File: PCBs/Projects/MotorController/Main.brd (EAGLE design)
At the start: 172.7 x 115.2 mm, 112 parts, among them Q1 ZXMP10A17GQ, Q2 BUK9240-100A.118, Q3 BUK9240-100A.118, Q4 MMBT5551LT1G, U1 LT4356-2, U2 DRV8301, U3 ESDA6V1SC6Y, U4 MTI85W100GC, U5 ESDA6V1SC6Y, U7 ESDA6V1SC6Y, U8 TMP101, U9 ACS758LCB

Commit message: Schematic in eagle finished -decided to stick with eagle for the time being since the kicad switchover would take a lot of time -freewheeling diodes switched to vertical packages -footprint for psoc module completed -inductor package fixed -rgb led decided on and part made -changed abc order of connector j3 -part renumbering
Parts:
- removed 10U: 47u, SparkFun-Capacitors:1210
- removed D14: LED-RGB-CC-THRUDIFFUSE, SparkFun-LED:LED-RGB-THRU
- removed H1, H2, H3, H4, H5, H6: STAND-OFF, SparkFun-Electromechanical:STAND-OFF
- removed J6: (no value), connectorsTVD:2X03_MINIFIT_JR
- removed U8: TMP101, SparkFun-DigitalIC:SOT23-6
- removed U9: ACS758LCB, IC:CB5PIN
- added C28: 0.1u, SparkFun-Capacitors:0805
- added D12: MBRF1090, SparkFun-DiscreteSemi:TO220V_2
- added J5: (no value), connectorsTVD:2X03_MINIFIT_JR
- added R41: 1M, SparkFun-Resistors:1206
- added S1, S2, S3, S4, S5, S6: STANDOFF_ELECTRICAL, SparkFun-Electromechanical:STANDOFF-ELECTRICAL
- added SJ1: SOLDERJUMPERTRACE, SparkFun-Retired:SJ_2S-TRACE
- added U11: LT4356-2, IC:SOIC-16
- added U6: ESDA6V1SC6Y, IC:SOT23-6
- C10: value 4.7u -> 0.1u; device SparkFun-Capacitors:1210 -> SparkFun-Capacitors:0805
- C11: value 0.1u -> 22n
- C12: value 47u -> 4.7u
- C13: value 47u -> 0.1u; device SparkFun-Capacitors:1210 -> SparkFun-Capacitors:0805
- C14, C19: value 22n -> 0.1u
- C15: value 2.2u -> 0.1u; device SparkFun-Capacitors:1210 -> SparkFun-Capacitors:0805
- C17: value 4.7u -> 2.2u
- C18: value 0.01u -> 4.7u; device SparkFun-Capacitors:0805 -> SparkFun-Capacitors:1210
- C2: value 4.7u -> 47n; device SparkFun-Passives:1210 -> SparkFun-Capacitors:0805
- C20, C21, C22: value 0.1u -> 47u; device SparkFun-Capacitors:0805 -> SparkFun-Capacitors:1210
- C23: value 10n -> 0.01u
- C24: value 10n -> 0.1u
- C26, C27: value 0.1u -> 10n
- C3: value 120P -> 4.7u; device SparkFun-Capacitors:0805 -> SparkFun-Passives:1210
- C4: value 47n -> 6.8N
- C5: value 6.8N -> 120P
- C6: value 1u -> 22n
- C8: value 0.1u -> 1u
- D1: value SMAJ70CA -> RED; device SparkFun-DiscreteSemi:SMA-DIODE -> SparkFun-LED:LED-1206
- D10, D11, D7, D8: device SparkFun-DiscreteSemi:TO-220H_2 -> SparkFun-DiscreteSemi:TO220V_2
- D2: value PMEG10030ELPX -> S3BB
- D3: value MBRF1090 -> S3BB; device SparkFun-DiscreteSemi:TO-220H_2 -> SparkFun-DiscreteSemi:SMB-DIODE
- D4: value S3BB -> SMAJ70CA; device SparkFun-DiscreteSemi:SMB-DIODE -> SparkFun-DiscreteSemi:SMA-DIODE
- D5: value S3BB -> PMEG10030ELPX
- D6: value MBRF1090 -> CLV1A-FKB; device SparkFun-DiscreteSemi:TO-220H_2 -> SparkFun-LED:P-LCC-4-3
- D9: value RED -> MBRF1090; device SparkFun-LED:LED-1206 -> SparkFun-DiscreteSemi:TO220V_2
- J1: device connectorsTVD:2X03_MINIFIT_JR -> connectorsTVD:MINIFIT_SR
- J2: device connectorsTVD:MINIFIT_SR -> connectorsTVD:2X03_MINIFIT_JR
- L1: device SparkFun-Passives:CDRH125 -> SparkFun-Passives:IND_SMD_SRP7050TA
- MOD1: value PSOC5LP-DEVBRD -> PSOC5LP-DEVBRDCY8CKIT-059; device modules:TQFP100 -> modules:CYKIT059
- Q2: value BUK9240-100A.118 -> MMBT5551LT1G; device SparkFun-DiscreteSemi:DPAK -> SparkFun-DiscreteSemi:SOT23-3
- Q4: value MMBT5551LT1G -> BUK9240-100A.118; device SparkFun-DiscreteSemi:SOT23-3 -> SparkFun-DiscreteSemi:DPAK
- R1: value 274K -> 2.8k
- R10: value 250k -> 10
- R11: value 100 -> 274K; device SparkFun-Resistors:0805 -> SparkFun-Resistors:1206
- R12: value 10k -> 4.99K; device SparkFun-Resistors:0805 -> SparkFun-Resistors:1206
- R13: value 51k -> 16.2K
- R14: value 47k -> 250k
- R15: value 10k -> 47k
- R16: value 10k -> 100
- R17: value 0.016 -> 51k; device SparkFun-Resistors:R2010 -> SparkFun-Resistors:0805
- R18: value 51 -> 10k; device SparkFun-Resistors:1206 -> SparkFun-Resistors:0805
- R19: value 30k -> 10; device SparkFun-Resistors:1206 -> SparkFun-Resistors:0805
- R2: value 10 -> 30k
- R20: value 2.8k -> 100; device SparkFun-Resistors:1206 -> SparkFun-Resistors:0805
- R21: value 100k -> 100; device SparkFun-Resistors:1206 -> SparkFun-Resistors:0805
- R22: value 5.1k -> 330; device SparkFun-Resistors:1206 -> SparkFun-Resistors:0805
- R23: value 10k -> 330; device SparkFun-Passives:1206 -> SparkFun-Resistors:0805
- R24: value 10k -> 330
- R25, R29: value 1k -> 100
- R3: value 1M -> 51; device SparkFun-Resistors:0805 -> SparkFun-Resistors:1206
- R30: value 330 -> 100
- R31: value 330 -> 510k
- R32: value 330 -> 1k
- R33: value 510k -> 1k
- R34, R35: value 100 -> 4.7k
- R36, R37, R38: value 100 -> 10k
- R39: value 4.7k -> 100k; device SparkFun-Resistors:0805 -> SparkFun-Resistors:1206
- R4: value 10 -> 10k; device SparkFun-Resistors:0805 -> SparkFun-Passives:1206
- R40: value 4.7k -> 5.1k; device SparkFun-Resistors:0805 -> SparkFun-Resistors:1206
- R5: device SparkFun-Resistors:0805 -> SparkFun-Resistors:1206
- R8: value 4.99K -> 0.016; device SparkFun-Resistors:1206 -> SparkFun-Resistors:R2010
- R9: value 16.2K -> 1M
- U1: value LT4356-2 -> DRV8301; device IC:SOIC-16 -> IC:HTSSOP_56
- U2: value DRV8301 -> ESDA6V1SC6Y; device IC:HTSSOP_56 -> IC:SOT23-6
- U4: value MTI85W100GC -> TMP101; device IC:ISOPLUS-DIL -> SparkFun-DigitalIC:SOT23-6
- U5: value ESDA6V1SC6Y -> ACS758LCB; device IC:SOT23-6 -> IC:CB5PIN
- U7: value ESDA6V1SC6Y -> MTI85W100GC; device IC:SOT23-6 -> IC:ISOPLUS-DIL
- moved U3 272.9 mm to (143.5, 10.2)
- moved D9 252.3 mm to (-223.5, -86.4)
- moved D8 246.3 mm to (-223.5, -66.0)
- moved D11 240.7 mm to (-223.5, -96.5)
- moved D10 239.2 mm to (-223.5, -76.2)
- moved Q1 216.9 mm to (78.7, 120.7)
- moved U5 211.5 mm to (106.7, 99.1), turned to 270 degrees
- moved Q4 192.3 mm to (59.7, 108.0)
- moved Q3 182.6 mm to (71.1, 108.0)
- moved U7 182.4 mm to (55.9, 57.1)
- moved L1 153.9 mm to (-226.1, 5.08)
- moved D7 144.7 mm to (-223.5, -55.9)
- moved R23 121.9 mm to (-137.2, 149.9)
- moved D6 119.1 mm to (-218.4, 5.08)
- moved R31 118.2 mm to (-19.1, 153.7)
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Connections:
- new net N$46: SJ1.1, U11.11
- net !CS: now also MOD1.36, U1.8; no longer U2.8
- net !FAULT: now also MOD1.44, U1.6; no longer U2.6
- net !IN-FAULT: now also U11.10; no longer U1.10
- net !OCTW: now also MOD1.43, U1.5; no longer U2.5
- net 3.3V: now also C9.1, U1.49; no longer C19.1, U2.49
- net 5V: now also C22.1, C28.1, D6.2, J5.5, MOD1.26, MOD1.52, R15.2, R17.2, R32.1, R34.1, R35.1, R36.1, R37.1, R38.1, U4.4, U6.1; no longer 10U.1, C18.1, J6.5, R13.2, R14.2, R15.1, R16.1, R24.1, R29.1, R39.1, R40.1, U8.4, U9.1
- net A: now also C13.2, D7.2, J3.3_1, J3.3_2, U1.46, U7.L1, U7.S1; no longer C22.2, D6.2, J3.1_1, J3.1_2, U2.46, U4.L1, U4.S1
- net B: now also C14.2, D9.2, U1.41, U7.L2, U7.S3; no longer C21.2, D3.2, U2.41, U4.L2, U4.S3
- net BUCK-EN: now also SJ1.2, U1.55; no longer U1.11, U2.55
- net C: now also C15.2, D11.2, D12.1, J3.1_1, J3.1_2, U1.36, U7.L3, U7.S5; no longer C20.2, D11.1, D7.2, J3.3_1, J3.3_2, U2.36, U4.L3, U4.S5
- net DISABLE: now also J2.4; no longer J1.4
- net DISP_OUT: now also J4.6, R21.1, U3.4; no longer J6.6, R36.1, U7.4
- net EN_GATE: now also MOD1.45, U1.16; no longer MOD1.12, U2.16
- net FB: now also R11.1, R12.2, U11.2; no longer R1.1, R8.2, U1.2
- net GATEDRV: now also R10.1, R9.2, U11.5; no longer R3.2, R4.1, U1.5
- net GH_A: now also U1.47, U7.G1; no longer U2.47, U4.G1
- net GH_B: now also U1.42, U7.G3; no longer U2.42, U4.G3
- net GH_C: now also U1.37, U7.G5; no longer U2.37, U4.G5
- net GL_A: now also U1.45, U7.G2; no longer U2.45, U4.G2
- net GL_B: now also U1.40, U7.G4; no longer U2.40, U4.G4
- net GL_C: now also U1.35, U7.G6; no longer U2.35, U4.G6
- net GND: now also C17.2, C18.1, C20.2, C21.2, C23.2, C24.2, C28.2, D12.2, D3.A, D4.C, J1.2_1, J1.2_2, J4.2, J5.4, J5.6, MOD1.25, MOD1.51, R1.1, R14.1, R16.2, R18.1, R19.2, R31.2, R40.1, R41.1, U1.28, U1.30, U1.31, U1.32, U1.33, U1.34, U1.39, U1.44, U1.EXP, U11.12, U2.2, U2.5, U4.2, U4.5, U6.2, U6.5, U7.L-, U7.S2, U7.S4, U7.S6; no longer C13.2, C15.2, C16.2, C17.1, C18.2, C26.2, C27.2, D1.C, D11.2, D14.2, D2.A, J2.2_1, J2.2_2, J4.4, J4.6, J6.2, R10.1, R11.2, R20.1, R22.1, R25.2, R5.2, R8.1, U1.12, U2.28, U2.30, U2.31, U2.32, U2.33, U2.34, U2.39, U2.44, U2.EXP, U4.L-, U4.S2, U4.S4, U4.S6, U5.5, U7.2, U7.5, U8.2, U8.5, U9.2
- net GPIO_TBD: now also J4.4, R20.1, U3.6; no longer J6.4, R35.1, U7.6
- net H1: now also C25.2, J5.1, R36.2; no longer C23.2, J4.1, R15.2
- net H2: now also C26.2, J5.2, R37.2; no longer C24.2, J4.2, R16.2
- net H3: now also C27.2, J5.3, R38.2; no longer C25.2, J4.3, R24.2
- net INH_A: now also MOD1.49, U1.17; no longer U2.17
- net INH_B: now also MOD1.27, U1.19; no longer U2.19
- net INH_C: now also MOD1.29, U1.21; no longer U2.21
- net INL_A: now also MOD1.50, U1.18; no longer U2.18
- net INL_B: now also MOD1.28, U1.20; no longer U2.20
- net INL_C: now also MOD1.30, U1.22; no longer U2.22
- net ISENSE: now also MOD1.3, U2.6, U5.3; no longer MOD1.27, U3.6, U9.3
- net MISO: now also MOD1.38, U1.10; no longer U2.10
- net MONITOR_RX: now also J4.3, R30.1, U3.3; no longer J6.3, R38.1, U7.3
- net MONITOR_TX: now also J4.1, R29.1, U3.1; no longer J6.1, R37.1, U7.1
- net MOSI: now also MOD1.39, U1.9; no longer U2.9
- net N$1: now also C2.1, U11.1; no longer C4.1, U1.1
- net N$10: now also C8.1, U1.27; no longer C7.1, U2.27
- net N$11: now also Q4.1, R10.2; no longer Q3.1, R4.2
- net N$12: now also C6.1, U1.56; no longer C9.1, U2.56
- net N$13: now also U11.16; no longer U1.16
- net N$14: now also R17.1, R18.2, U1.3; no longer R12.2, R13.1, U2.3
- net N$15: now also C16.1, U1.52; no longer C11.1, U2.52
- net N$16: now also C16.2, D5.C, L1.P$1, U1.50, U1.51; no longer C11.2, D2.C, L1.1, U2.50, U2.51
- net N$17: now also C11.2, U1.15; no longer C14.2, U2.15
- net N$18: now also C11.1, U1.14; no longer C14.1, U2.14
- net N$19: now also R2.1, R3.1; no longer R18.1, R19.1
- net N$2: now also R14.2, U1.1; no longer R10.2, U2.1
- net N$20: now also Q2.3, R5.1, R9.1; no longer Q4.3, R2.1, R3.1
- net N$21: now also C17.1, U1.13; no longer C15.1, U2.13
- net N$22: now also D1.A; no longer D9.A
- net N$23: now also D3.C, R4.1; no longer D5.C, R23.1
- net N$24: now also C13.1, U1.48; no longer C22.1, U2.48
- net N$25: now also C15.1, U1.38; no longer C20.1, U2.38
- net N$26: now also R16.1, U1.7; no longer R11.1, U2.7
- net N$27: now also MOD1.10; no longer MOD1.42
- net N$28: now also MOD1.11; no longer MOD1.43
- net N$29: now also MOD1.12; no longer MOD1.44
- net N$3: now also C4.1, R13.2; no longer C5.1, R9.2
- net N$30: now also C14.1, U1.43; no longer C21.1, U2.43
- net N$31: now also R41.2, S1.P1; no longer MOD1.49, MOD1.50
- net N$32: now also MOD1.34, R24.1; no longer MOD1.25, R30.1
- net N$33: now also MOD1.33, R23.1; no longer MOD1.24, R31.1
- net N$34: now also MOD1.32, R22.1; no longer MOD1.23, R32.1
- net N$35: now also D6.1, R24.2; no longer D14.1, R30.2
- net N$36: now also D6.4, R23.2; no longer D14.3, R31.2
- net N$37: now also D6.3, R22.2; no longer D14.4, R32.2
- net N$38: now also C20.1, C21.1, L1.P$2; no longer C12.1, C13.1, L1.2
- net N$39: now also MOD1.6, R25.2; no longer MOD1.30, R34.2
- net N$4: now also D1.C, R1.2; no longer D9.C, R20.2
- net N$40: now also C22.2, R19.1; no longer 10U.2, R5.1
- net N$41: now also MOD1.47, R21.2; no longer MOD1.14, R36.2
- net N$42: now also MOD1.46, R20.2; no longer MOD1.13, R35.2
- net N$43: now also MOD1.14, R29.2; no longer MOD1.46, R37.2
- net N$44: now also MOD1.15, R30.2; no longer MOD1.47, R38.2
- net N$5: now also C7.1, U1.23; no longer C6.1, U2.23
- net N$6: now also C5.1, R13.1, U1.2; no longer C3.1, R9.1, U2.2
- net N$7: now also Q3.1, R5.2; no longer Q2.1, R2.2
- net N$8: now also D2.A, Q2.2, Q3.3; no longer D4.A, Q2.3, Q4.2
- net N$9: now also D2.C, Q2.1, R4.2; no longer D4.C, Q4.1, R23.2
- net POST-SENSE: now also Q4.4, R8.2, U11.7; no longer Q3.4, R17.2, U1.7
- net PRE-SENSE: now also D4.A, Q3.4, R8.1, U11.8, U11.9; no longer D1.A, Q2.4, R17.1, U1.8, U1.9
- net PRESENSE: now also R2.2; no longer R19.2
- net PWRGD: now also R15.1, U1.4; no longer R14.1, U2.4
- net REVERSE: now also J2.6; no longer J1.6
- net SCL: now also MOD1.42, R34.2, U4.1; no longer MOD1.34, R39.2, U8.1
- net SCLK: now also MOD1.37, U1.11; no longer U2.11
- net SDA: now also MOD1.41, R35.2, U4.6; no longer MOD1.35, R40.2, U8.6
- net THROTTLE_1: now also J2.1, R32.2, U2.1; no longer J1.1, R29.2, U3.1
- net THROTTLE_2: now also J2.2, R25.1, R31.1, U2.3; no longer J1.2, R33.1, R34.1, U3.3
- net THROTTLE_3: now also J2.3, R33.1; no longer J1.3, R25.1
- net T_ALERT: now also MOD1.40, U4.3; no longer MOD1.36, U8.3
- net UNDERVOLTAGE: now also R3.2, U11.14; no longer R18.2, U1.14
- net VCC: now also C12.1, C18.2, C19.1, C3.1, Q4.3, R11.2, R39.2, U1.29, U1.53, U1.54, U11.4; no longer C16.1, C17.2, C2.1, C8.1, Q3.3, R1.2, R21.2, U1.4, U2.29, U2.53, U2.54
- net VIN: now also J1.1_1, J1.1_2, U5.4_1, U5.4_2, U5.4_3, U5.4_4, U5.4_5, U5.4_6, U5.4_7, U5.4_8; no longer J2.1_1, J2.1_2, U9.4_1, U9.4_2, U9.4_3, U9.4_4, U9.4_5, U9.4_6, U9.4_7, U9.4_8
- net VSENSE: now also MOD1.2, R39.1, R40.2, U2.4; no longer MOD1.26, R21.1, R22.2, U3.4
- net V_BATT: now also D11.1, D9.1, U5.5_1, U5.5_2, U5.5_3, U5.5_4, U5.5_5, U5.5_6, U5.5_7, U5.5_8, U7.L+; no longer D3.1, D6.1, U4.L+, U9.5_1, U9.5_2, U9.5_3, U9.5_4, U9.5_5, U9.5_6, U9.5_7, U9.5_8
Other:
- board size 172.7 x 115.2 mm -> 172.7 x 138.1 mm

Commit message: PCB layout progress -completed first revision of input protection -added drc file which added 2 more layers and modified parameters of sparkfun's stock DRC -corrected schematic error which listed labeled a net presense not pre-sense
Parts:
- added SJ2: SOLDERJUMPERNO, SparkFun-Retired:SJ_2S-NO
- moved D12 347.0 mm to (-17.8, 172.7), turned to 90 degrees
- moved D11 332.8 mm to (-27.9, 172.7), turned to 90 degrees
- moved D9 318.6 mm to (-38.1, 172.7), turned to 90 degrees
- moved D10 304.4 mm to (-48.3, 172.7), turned to 90 degrees
- moved L1 296.0 mm to (54.6, 99.1)
- moved D8 290.3 mm to (-58.4, 172.7), turned to 90 degrees
- moved D7 276.2 mm to (-68.6, 172.7), turned to 90 degrees
- moved R41 275.9 mm to (38.1, 22.2), turned to 90 degrees
- moved S1 266.3 mm to (38.1, 28.6), turned to 90 degrees
- moved Q2 262.8 mm to (132.1, 117.5)
- moved S6 257.8 mm to (-81.3, 170.2), turned to 90 degrees
- moved D4 249.7 mm to (114.3, 122.6), turned to 90 degrees
- moved C3 247.6 mm to (104.8, 101.0), turned to 270 degrees
- moved S5 247.3 mm to (-88.9, 170.2), turned to 90 degrees
- moved C1 239.5 mm to (101.6, 101.0), turned to 270 degrees
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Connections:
- removed net N$8: D2.A, Q2.2, Q3.3
- removed net PRESENSE: Q1.3, R2.2
- new net PREJUMP_5V: C22.1, C23.1, L2.1, SJ2.1
- net 5V: now also SJ2.2; no longer C22.1, C23.1, L2.1
- net PRE-SENSE: now also Q1.3, R2.2
- net V_BATT: now also D2.A, Q2.2, Q3.3
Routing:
- net N$20: track 0.00 -> 44.3 mm, vias 0 -> 2
- net N$13: track 0.00 -> 32.5 mm, vias 0 -> 2
- net PRE-SENSE: track 0.00 -> 29.3 mm, vias 0 -> 2
- net GATEDRV: track 0.00 -> 24.6 mm, vias 0 -> 2
- net FB: track 0.00 -> 22.6 mm, vias 0 -> 2
- net V_BATT: track 0.00 -> 18.4 mm
- net N$22: track 0.00 -> 13.4 mm
- net UNDERVOLTAGE: track 0.00 -> 12.8 mm, vias 0 -> 2
- net VCC: track 0.00 -> 12.3 mm
- net N$19: track 0.00 -> 7.74 mm
- net POST-SENSE: track 0.00 -> 6.56 mm, vias 0 -> 1
- net N$9: track 0.00 -> 6.48 mm
- net N$7: track 0.00 -> 5.45 mm
- net N$23: track 0.00 -> 3.81 mm
- net N$11: track 0.00 -> 3.52 mm
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- added copper zone on layer 1, net POST-SENSE
- added copper zone on layer 1, net PRE-SENSE
- added copper zone on layer 1, net VCC

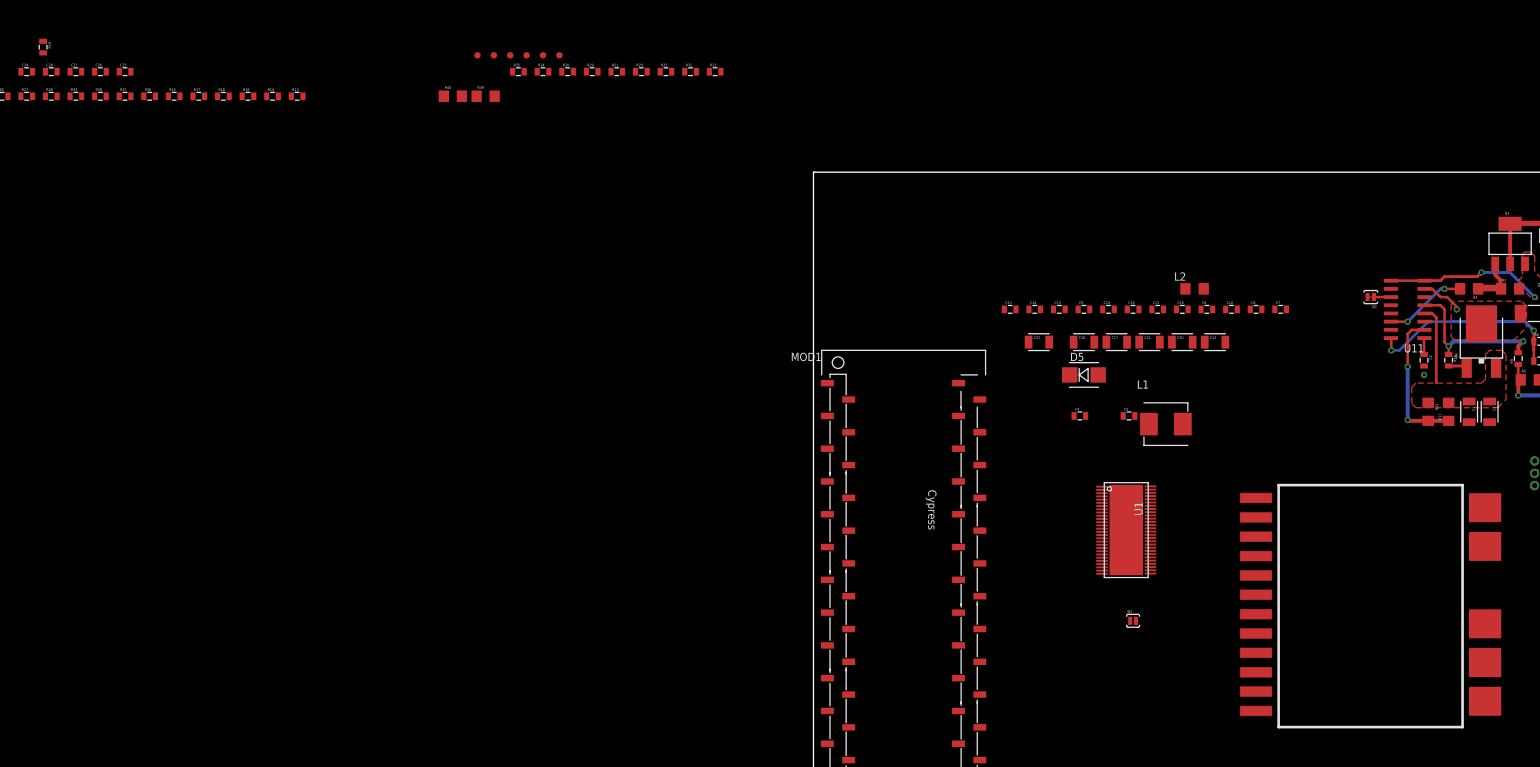
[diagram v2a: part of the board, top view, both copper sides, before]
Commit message: More work done on the buck converter of the drv8301
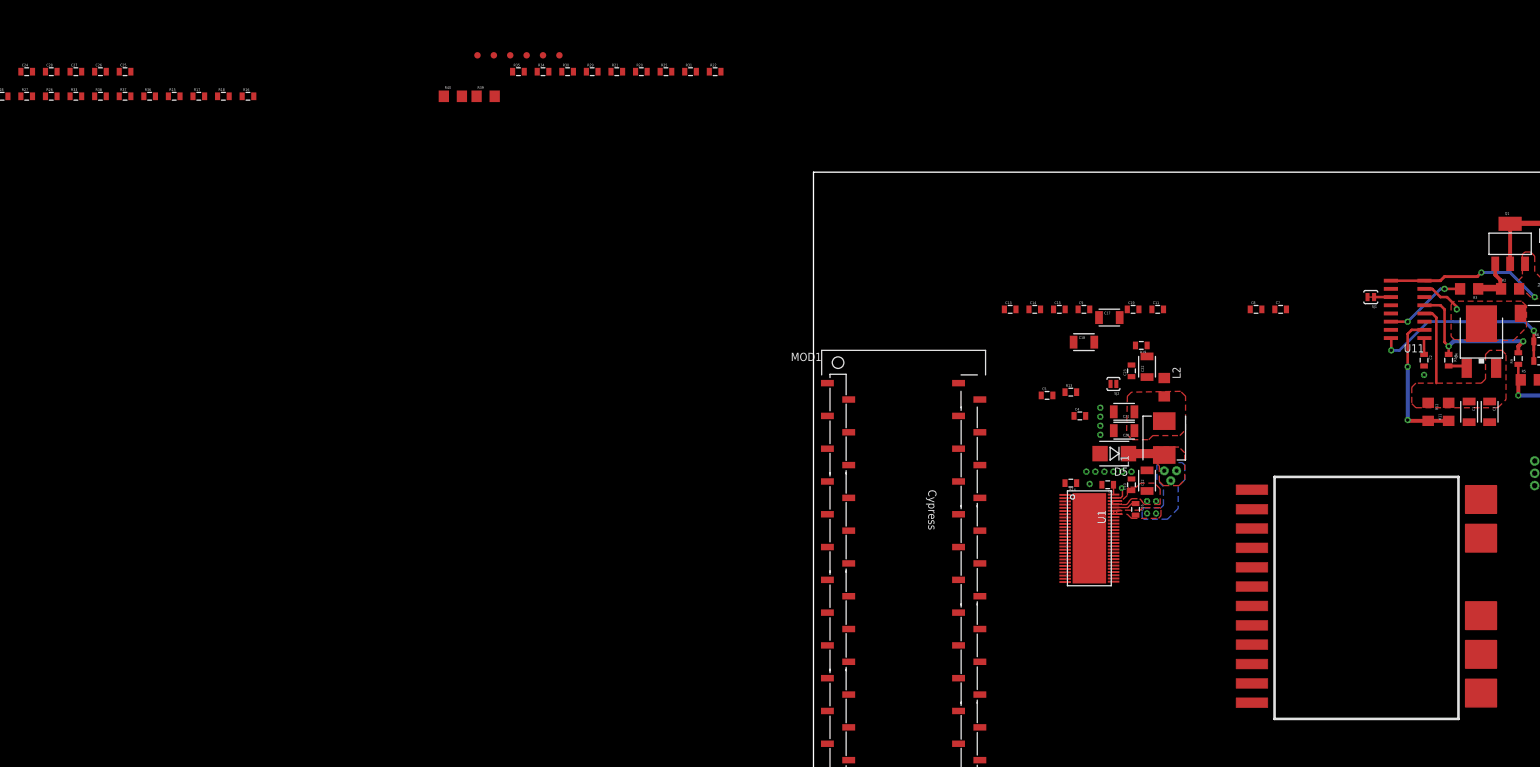
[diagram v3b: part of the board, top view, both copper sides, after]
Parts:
- moved R19 176.3 mm to (50.8, 111.3), turned to 180 degrees
- moved R14 137.5 mm to (39.9, 89.9), turned to 180 degrees
- moved R13 128.4 mm to (39.9, 104.0)
- moved SJ2 36.8 mm to (46.5, 105.3), turned to 180 degrees
- moved C16 31.8 mm to (49.9, 85.9), turned to 270 degrees
- moved C10 31.3 mm to (49.3, 89.7), turned to 90 degrees
- moved C6 31.2 mm to (45.6, 89.7), turned to 180 degrees
- moved C12 23.9 mm to (51.7, 90.3), turned to 90 degrees
- moved C22 17.2 mm to (51.7, 108.0), turned to 90 degrees
- moved C20 16.4 mm to (48.1, 98.0), turned to 180 degrees
- moved L2 15.9 mm to (54.4, 104.8), turned to 270 degrees
- moved C5 13.1 mm to (36.2, 103.5)
- moved D5 13.1 mm to (46.6, 94.5), turned to 180 degrees
- moved C21 11.5 mm to (48.1, 101.0), turned to 180 degrees
- moved C23 10.2 mm to (49.3, 107.3), turned to 90 degrees
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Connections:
- net N$16 renamed IND_LOOP_IN
- net N$38 renamed IND_LOOP_OUT
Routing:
- net IND_LOOP_IN: track 0.00 -> 8.64 mm, vias 0 -> 5
- net N$15: track 0.00 -> 3.67 mm
- net BUCK-EN: track 0.00 -> 2.80 mm, vias 0 -> 1
- net VCC: track 12.3 -> 14.8 mm, vias 0 -> 2
- net N$12: track 0.00 -> 1.52 mm
- added copper zone on layer 1, net IND_LOOP_IN
- added copper zone on layer 16, net IND_LOOP_IN
- added copper zone on layer 1, net IND_LOOP_OUT

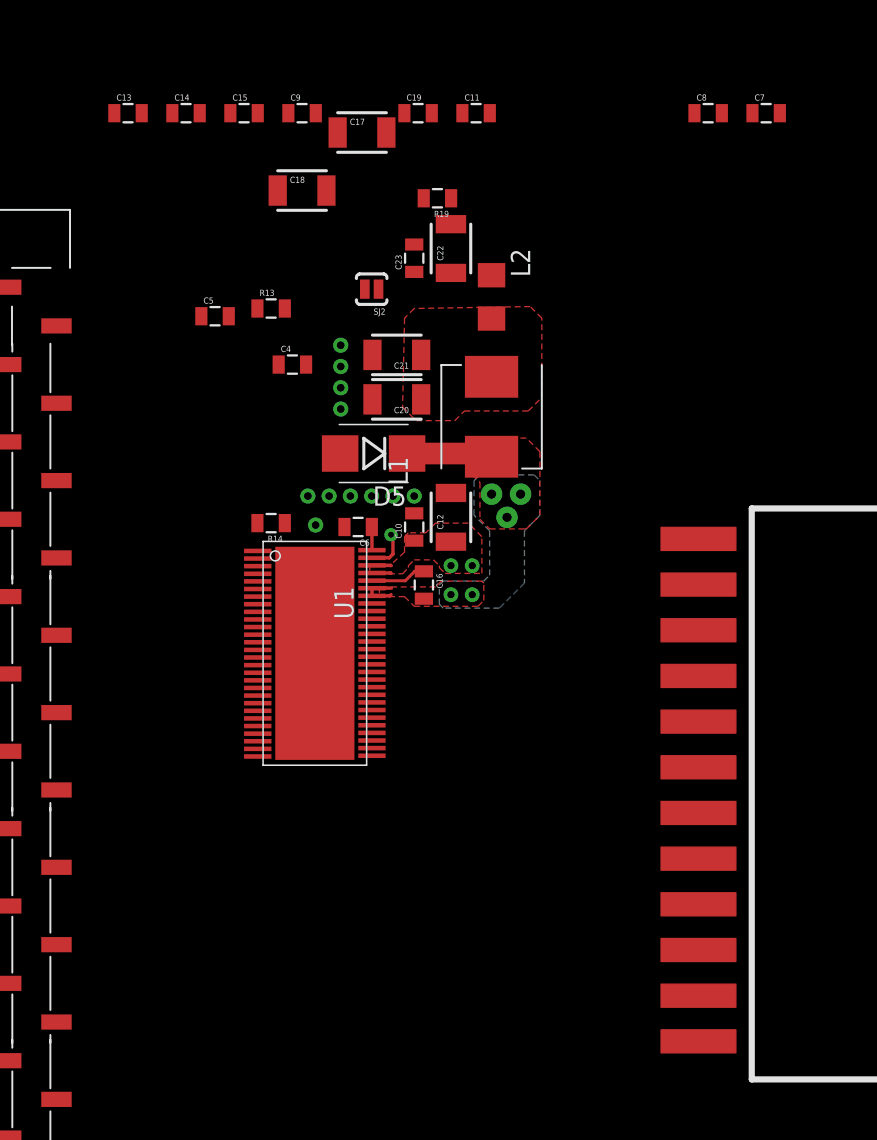
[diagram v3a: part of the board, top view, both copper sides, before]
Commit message: Finished gate driver layout -added the design rules check file that was omitted in a previous commit
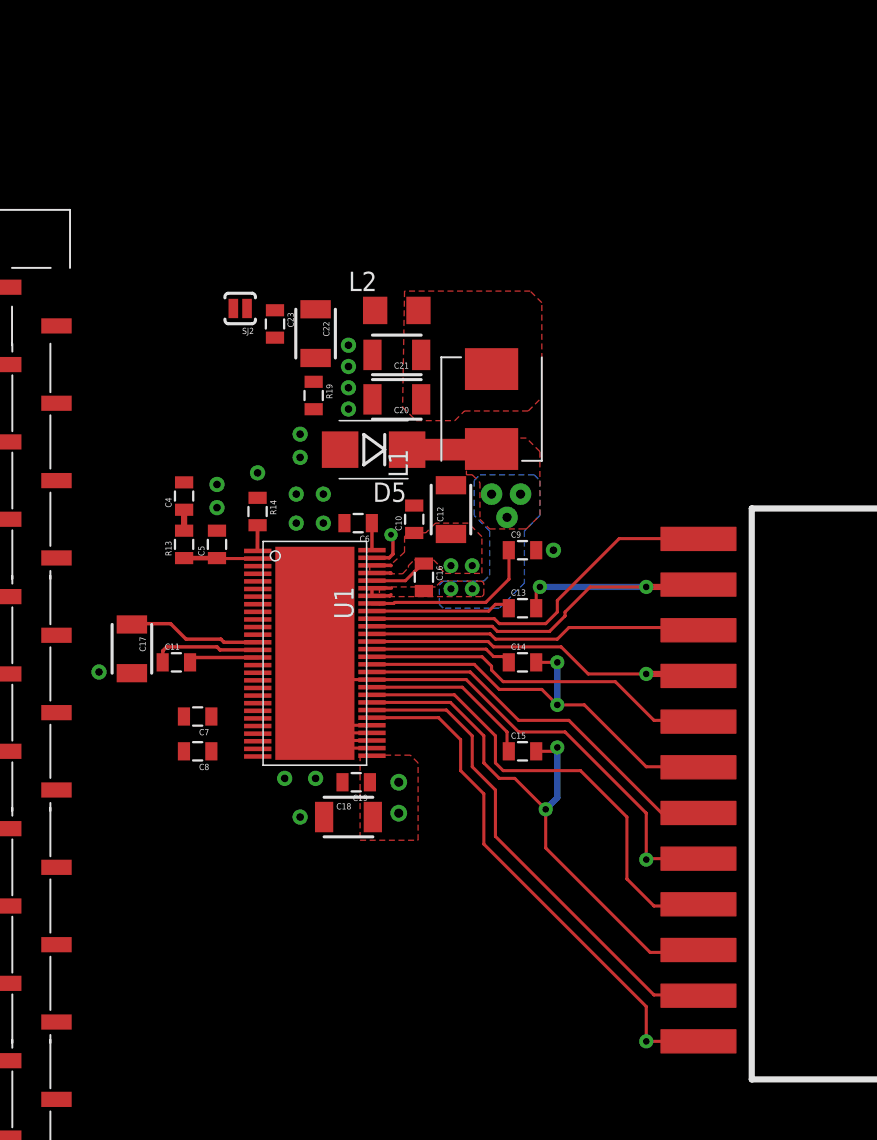
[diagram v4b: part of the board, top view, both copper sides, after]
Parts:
- moved C7 54.4 mm to (35.1, 77.2), turned to 180 degrees
- moved C8 53.7 mm to (35.1, 74.9), turned to 180 degrees
- moved C15 45.7 mm to (56.4, 74.9)
- moved C19 44.1 mm to (45.5, 72.9), turned to 180 degrees
- moved C14 42.3 mm to (56.4, 80.8)
- moved C13 41.6 mm to (56.4, 84.3)
- moved C18 41.3 mm to (45.0, 70.6)
- moved C11 41.1 mm to (33.7, 80.8)
- moved C17 37.1 mm to (30.7, 81.7), turned to 270 degrees
- moved C9 32.1 mm to (56.4, 88.1)
- moved R13 16.5 mm to (34.2, 88.5), turned to 90 degrees
- moved R19 15.3 mm to (42.7, 98.3), turned to 270 degrees
- moved C5 15.0 mm to (36.3, 88.5), turned to 90 degrees
- moved C4 11.2 mm to (34.2, 91.7), turned to 90 degrees
- moved C22 10.5 mm to (42.8, 102.4), turned to 270 degrees
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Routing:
- net GND: track 0.00 -> 122.4 mm, vias 4 -> 17
- net C: track 0.00 -> 36.7 mm, vias 0 -> 2
- net GL_C: track 0.00 -> 32.2 mm
- net A: track 0.00 -> 31.0 mm, vias 0 -> 2
- net GH_C: track 0.00 -> 30.7 mm
- net B: track 0.00 -> 29.7 mm, vias 0 -> 2
- net GL_B: track 0.00 -> 25.5 mm
- net GH_B: track 0.00 -> 23.4 mm
- net GH_A: track 0.00 -> 23.2 mm
- net GL_A: track 0.00 -> 22.0 mm
- net 3.3V: track 0.00 -> 11.6 mm
- net N$25: track 0.00 -> 11.4 mm
- net N$30: track 0.00 -> 9.35 mm
- net N$24: track 0.00 -> 9.28 mm
- net N$21: track 0.00 -> 8.79 mm
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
